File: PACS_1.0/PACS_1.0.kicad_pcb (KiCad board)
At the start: 2 copper layers, 73.6 x 42.7 mm, 47 parts, among them J1 Conn_01x04_Socket, J2 Conn_01x02_Pin, Q1 PN2222A, U1 MSP430G2553IN20, U2 S-80855CNMC-B9GT2U, U3 BSS84PH6327XTSA2, U4 TPS562201DDCR, U5 MCP9700Ax-ETT, U6 LTR-303ALS-01, U7 XB24CZ7WIT-004

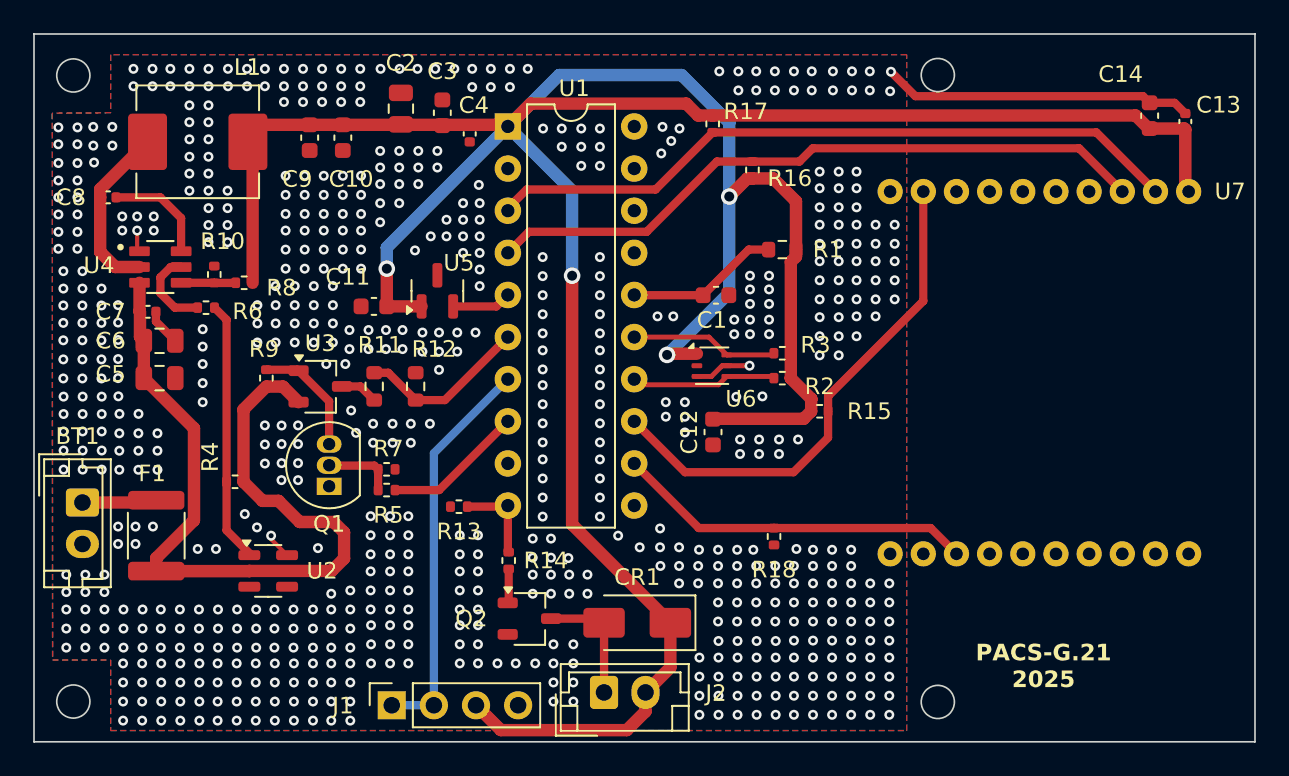
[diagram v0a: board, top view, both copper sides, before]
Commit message: Removed silkscreen from stitching vias
created new set of gerber files, revision 2.0
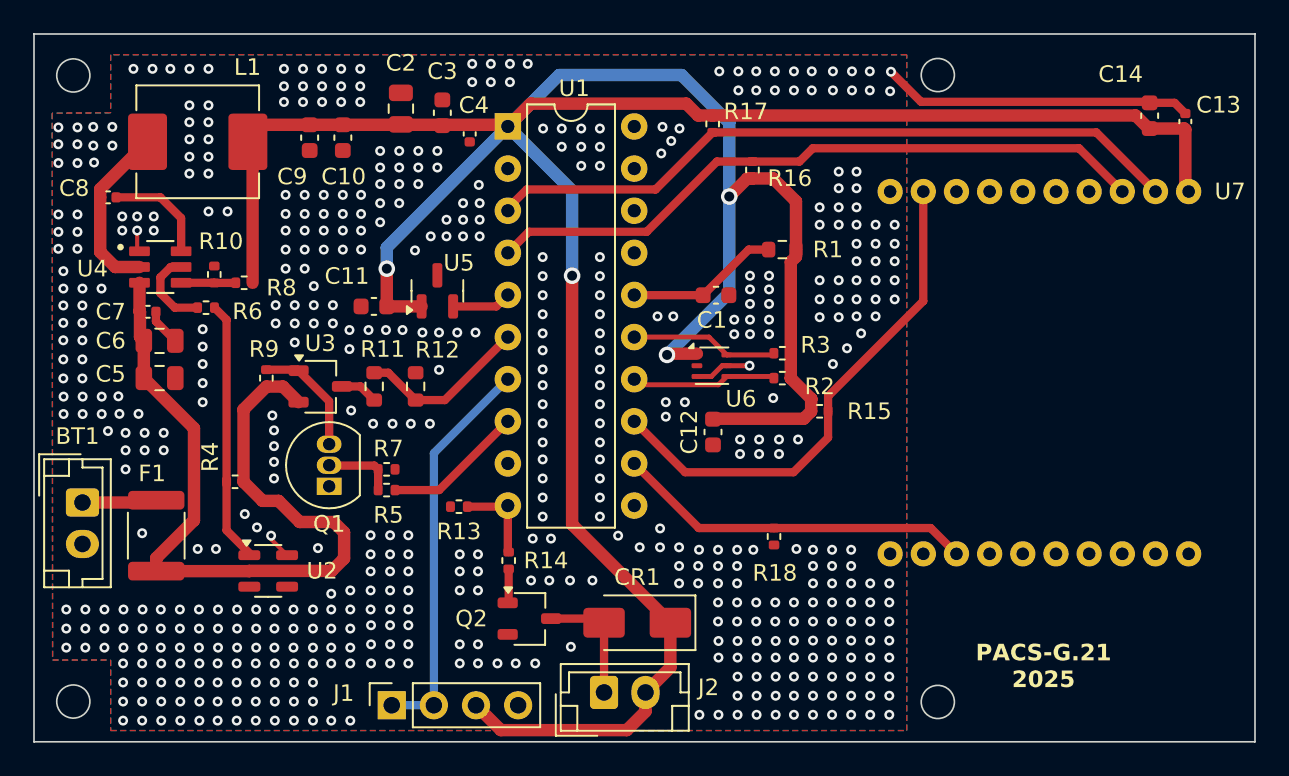
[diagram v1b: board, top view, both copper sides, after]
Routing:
- net GND: vias 692 -> 545
